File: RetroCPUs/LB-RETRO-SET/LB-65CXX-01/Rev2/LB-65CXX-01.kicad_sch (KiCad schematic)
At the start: 18 parts, among them J1 Conn_02x32_Odd_Even, J2 JUMPER, SW1 SW_Push, U1 W65C02_816S_DIP, U2 GAL16V8B, U3 OSC, U4 DS1813-5

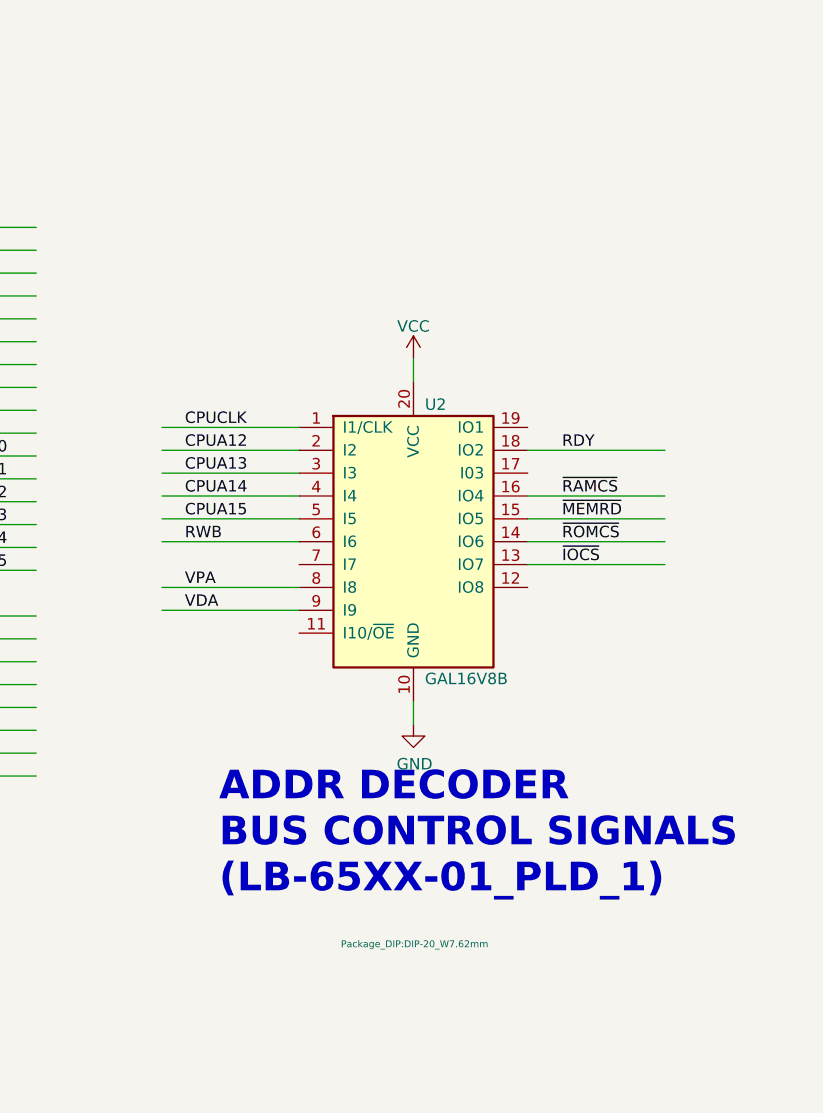
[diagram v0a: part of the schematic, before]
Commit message: Card updates - Add LEDs to CPU cards
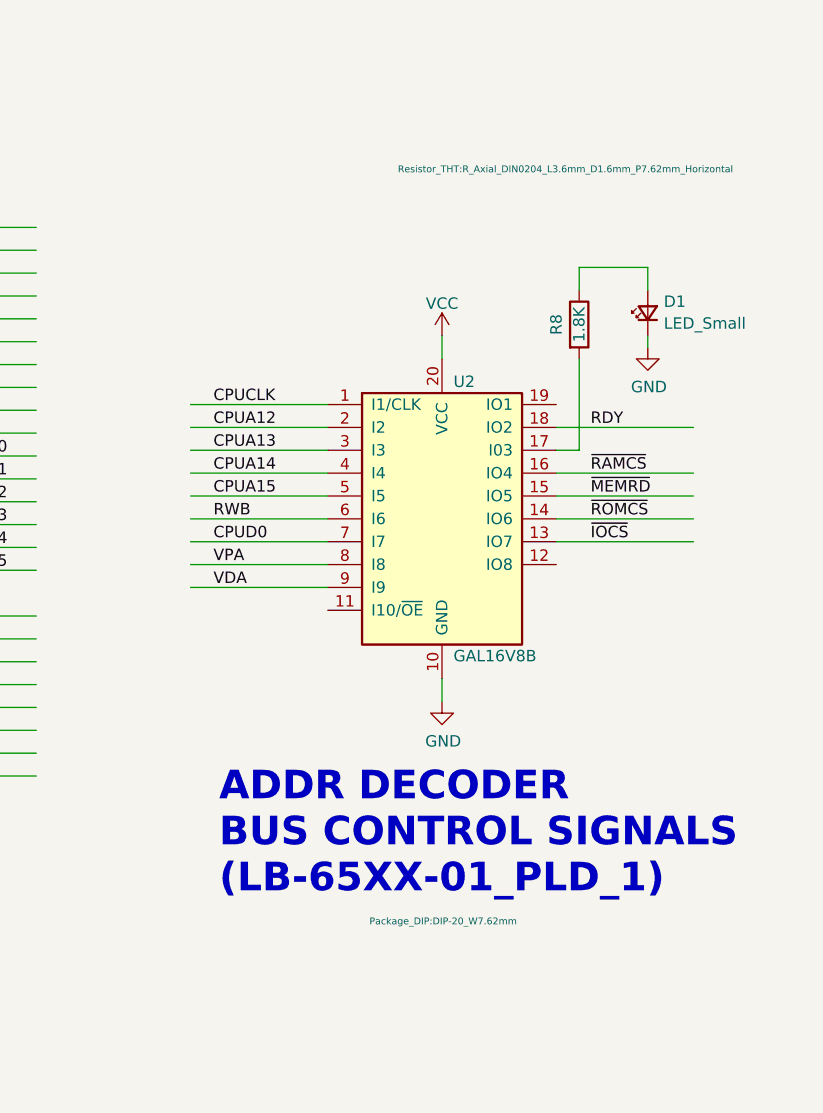
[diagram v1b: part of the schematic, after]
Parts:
- added D1: LED_Small, LED_THT:LED_D5.0mm_Horizontal_O3.81mm_Z9.0mm, symbol Device:LED_Small
- added R8: 1.8K, Resistor_THT:R_Axial_DIN0204_L3.6mm_D1.6mm_P7.62mm_Horizontal, symbol Device:R
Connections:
- net CPUD0: now also U2.7 (I7)
- net GND: now also D1.1 (K)
- net at U2.17 (I03): now also R8.2
- new net: D1.2 (A), R8.1
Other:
- moved on the sheet: U2
